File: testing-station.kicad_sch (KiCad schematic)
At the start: 15 parts, among them J1 pyranometer, J10 Conn_01x06_Socket, J11 Conn_01x08_Socket, J2 anemometer, J3 AM2315C, J4 FPC connector, J6 Conn_01x10_Socket, J8 Conn_01x08_Socket, SW1 500SSP1S2M2QEA, U1 TBA_1-0519

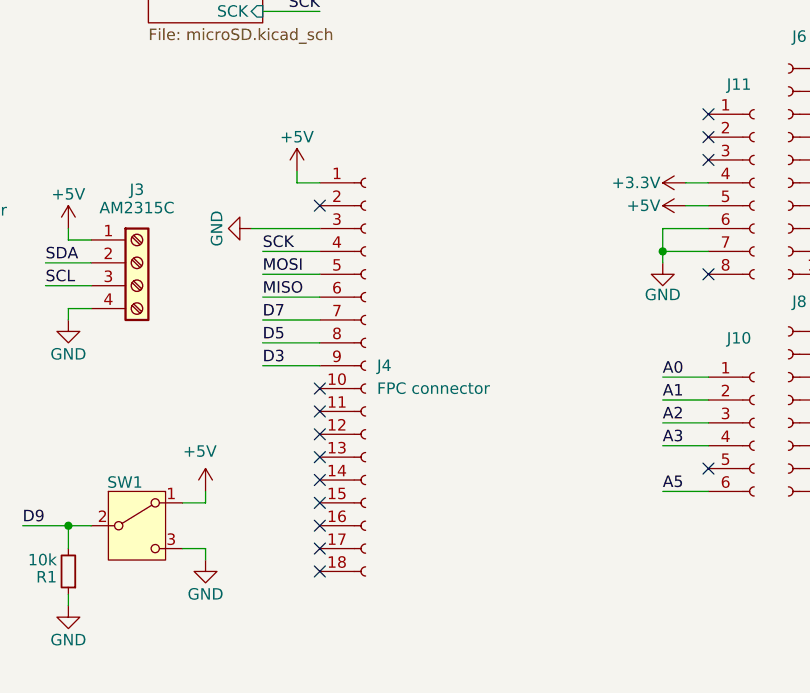
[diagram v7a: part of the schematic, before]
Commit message: implemented Eurocircuits design remarks
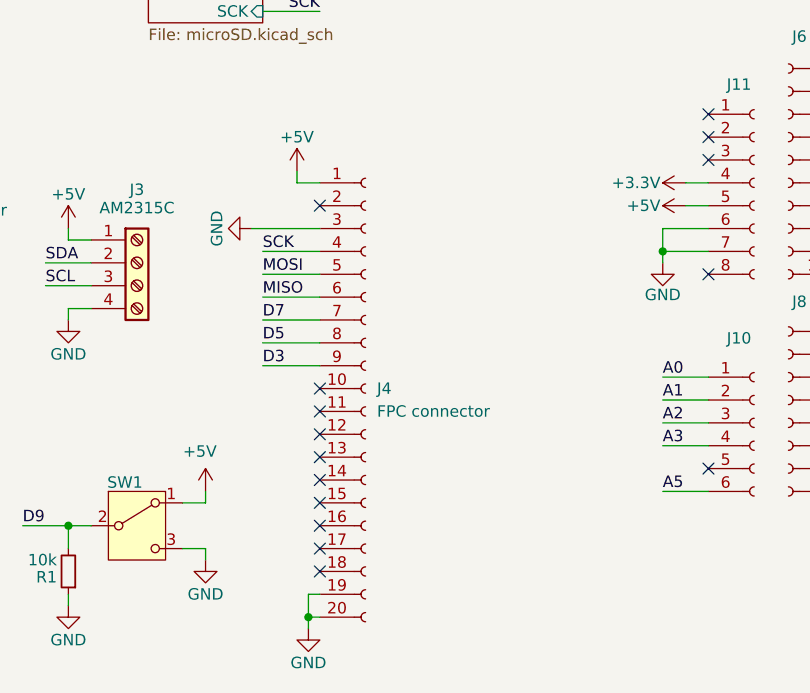
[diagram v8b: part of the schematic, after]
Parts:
- removed J4: FPC connector, external_footprints:XF2M-1815-1A, symbol Connector:Conn_01x18_Socket
- added J4: FPC connector, external_footprints:XF2M-1815-1A, symbol Connector:Conn_01x20_Socket
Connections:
- net +5V: now also J4.1 (Pin_1)
- net D3: now also J4.9 (Pin_9)
- net D5: now also J4.8 (Pin_8)
- net D7: now also J4.7 (Pin_7)
- net GND: now also J4.19 (Pin_19), J4.20 (Pin_20), J4.3 (Pin_3)
- net MISO: now also J4.6 (Pin_6)
- net MOSI: now also J4.5 (Pin_5)
- net SCK: now also J4.4 (Pin_4)
